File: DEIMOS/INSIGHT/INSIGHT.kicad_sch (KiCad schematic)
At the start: 78 parts, among them J1 Batt, J3 USB_C_Receptacle_USB2.0_16P, J4 Boot, J5 GND, SW3 SW_SPDT, U1 LSM6DS3, U2 MPL3115A2, U3 W25Q128JVSIQ, U4 BNO085, U5 RP2040, U6 Adafruit GPS, U7 MPM3610GQV-Z, U8 RFM95W-915S2, Y1 ABM8-272-T3, Y2 ABS07-32.768KHZ-1-T

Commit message: Finally got to a first footprint with insight it si 3:30 am signing off. There are a few issues and nothing is close to routed yet but it is good enough for now bigest change was putting the rfm95w side by side with the gps foot print is and will proably stay 1.5 x 3. Which is a 0.5 increase on all side to the COMET.
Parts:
- added J2: SMA-J-P-GF-RA-SM1, SMA-J-P-GF-RA-SM1:SAMTEC_SMA-J-P-GF-RA-SM1, symbol SMA-J-P-GF-RA-SM1:SMA-J-P-GF-RA-SM1
- D1, D4: footprint Diode_SMD:D_SOD-323F -> Diode_SMD:D_SOD-110
- J1: footprint Connector_JST:JST_EH_B2B-EH-A_1x02_P2.50mm_Vertical -> TerminalBlock_4Ucon:TerminalBlock_4Ucon_1x02_P3.50mm_Horizontal
- SW3: footprint SPDT:SW_500ASSP1SM6QE -> Button_Switch_SMD:SW_SPDT_CK_JS102011SAQN
- U4: footprint LGA-28_CEV -> footprints:LGA-28_CEV
- U8: footprint (none) -> RF_Module:HOPERF_RFM9XW_SMD
- Y2: footprint ABS07-32.768KHZ-1-T:XTAL_ABS07-32.768KHZ-1-T -> ABS07_32_768KHZ_1_T:XTAL_ABS07-32.768KHZ-1-T
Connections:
- new net: J2.2, J2.3, J2.4, J2.5
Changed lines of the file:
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@@
 	)
 	(rectangle
-		(start 703.58 349.25)
-		(end 824.23 426.72)
+		(start 734.695 349.25)
+		(end 814.705 426.72)
 		(stroke
 			(width 0.508)
@@
 	(text "RFM95W"
 		(exclude_from_sim no)
-		(at 764.032 423.926 0)
+		(at 765.048 414.782 0)
 		(effects
 			(font
@@
 			)
 		)
-		(property "Footprint" "LGA-28_CEV"
+		(property "Footprint" "footprints:LGA-28_CEV"
 			(at 731.52 300.99 0)
 			(hide yes)
@@
 			)
 		)
-		(property "Footprint" "Diode_SMD:D_SOD-323F"
+		(property "Footprint" "Diode_SMD:D_SOD-110"
 			(at 318.77 363.22 0)
 			(hide yes)
@@
 			)
 		)
-		(property "Footprint" "ABS07-32.768KHZ-1-T:XTAL_ABS07-32.768KHZ-1-T"
+		(property "Footprint" "ABS07_32_768KHZ_1_T:XTAL_ABS07-32.768KHZ-1-T"
 			(at 805.18 304.8 0)
 			(hide yes)
@@
 	)
 	(symbol
+		(lib_id "SMA-J-P-GF-RA-SM1:SMA-J-P-GF-RA-SM1")
+		(at 788.67 379.73 0)
+		(mirror y)
+		(unit 1)
+		(body_style 1)
+		(exclude_from_sim no)
+		(in_bom yes)
+		(on_board yes)
+		(in_pos_files yes)
+		(dnp no)
+		(property "Reference" "J2"
+			(at 789.051 370.84 0)
+			(show_name no)
+			(do_not_autoplace no)
+			(effects
+				(font
+					(size 1.27 1.27)
+				)
+			)
+		)
+		(property "Value" "SMA-J-P-GF-RA-SM1"
+			(at 789.051 373.38 0)
+			(show_name no)
+			(do_not_autoplace no)
+			(effects
+				(font
+					(size 1.27 1.27)
+				)
+			)
+		)
+		(property "Footprint" "SMA-J-P-GF-RA-SM1:SAMTEC_SMA-J-P-GF-RA-SM1"
+			(at 788.67 379.73 0)
+			(hide yes)
+			(show_name no)
+			(do_not_autoplace no)
+			(effects
+				(font
+					(size 1.27 1.27)
+				)
+				(justify bottom)
+			)
+		)
+		(property "Datasheet" ""
+			(at 788.67 379.73 0)
+			(hide yes)
+			(show_name no)
+			(do_not_autoplace no)
+			(effects
+				(font
+					(size 1.27 1.27)
+				)
+			)
+		)
+		(property "Description" ""
+			(at 788.67 379.73 0)
+			(hide yes)
+			(show_name no)
+			(do_not_autoplace no)
+			(effects
+				(font
+					(size 1.27 1.27)
+				)
+			)
+		)
+		(property "PARTREV" "D"
+			(at 788.67 379.73 0)
+			(hide yes)
+			(show_name no)
+			(do_not_autoplace no)
+			(effects
+				(font
+					(size 1.27 1.27)
+				)
+				(justify bottom)
+			)
+		)
+		(property "MANUFACTURER" "Samtec"
+			(at 788.67 379.73 0)
+			(hide yes)
+			(show_name no)
+			(do_not_autoplace no)
+			(effects
+				(font
+					(size 1.27 1.27)
+				)
+				(justify bottom)
+			)
+		)
+		(property "MAXIMUM_PACKAGE_HEIGHT" "9.99mm"
+			(at 788.67 379.73 0)
+			(hide yes)
+			(show_name no)
+			(do_not_autoplace no)
+			(effects
+				(font
+					(size 1.27 1.27)
+				)
+				(justify bottom)
+			)
+		)
+		(property "STANDARD" "Manufacturer Recommendations"
+			(at 788.67 379.73 0)
+			(hide yes)
+			(show_name no)
+			(do_not_autoplace no)
+			(effects
+				(font
+					(size 1.27 1.27)
+				)
+				(justify bottom)
+			)
+		)
+		(pin "5"
+		)
+		(pin "4"
+		)
+		(pin "3"
+		)
+		(pin "2"
+		)
+		(pin "1"
+		)
+		(instances
+			(project "INSIGHT"
+				(path "/bf4b749c-e7df-4d18-856a-a4f784e96f1a"
+					(reference "J2")
+					(unit 1)
+				)
+			)
+		)
+	)
+	(symbol
 		(lib_id "Device:C")
 		(at 354.33 386.08 0)
@@
 			)
 		)
-		(property "Footprint" ""
+		(property "Footprint" "RF_Module:HOPERF_RFM9XW_SMD"
 			(at 681.99 342.9 0)
 			(hide yes)
@@
 			)
 		)
-		(property "Footprint" "SPDT:SW_500ASSP1SM6QE"
+		(property "Footprint" "Button_Switch_SMD:SW_SPDT_CK_JS102011SAQN"
 			(at 306.07 339.09 0)
 			(hide yes)
@@
 			)
 		)
-		(property "Footprint" "Connector_JST:JST_EH_B2B-EH-A_1x02_P2.50mm_Vertical"
+		(property "Footprint" "TerminalBlock_4Ucon:TerminalBlock_4Ucon_1x02_P3.50mm_Horizontal"
 			(at 288.29 339.09 0)
 			(hide yes)
@@
 		(exclude_from_sim no)
 		(in_bom yes)
-		(on_board yes)
+		(on_board no)
 		(in_pos_files yes)
 		(dnp no)
@@
 			)
 		)
-		(property "Footprint" "Diode_SMD:D_SOD-323F"
+		(property "Footprint" "Diode_SMD:D_SOD-110"
 			(at 311.15 370.84 0)
 			(hide yes)

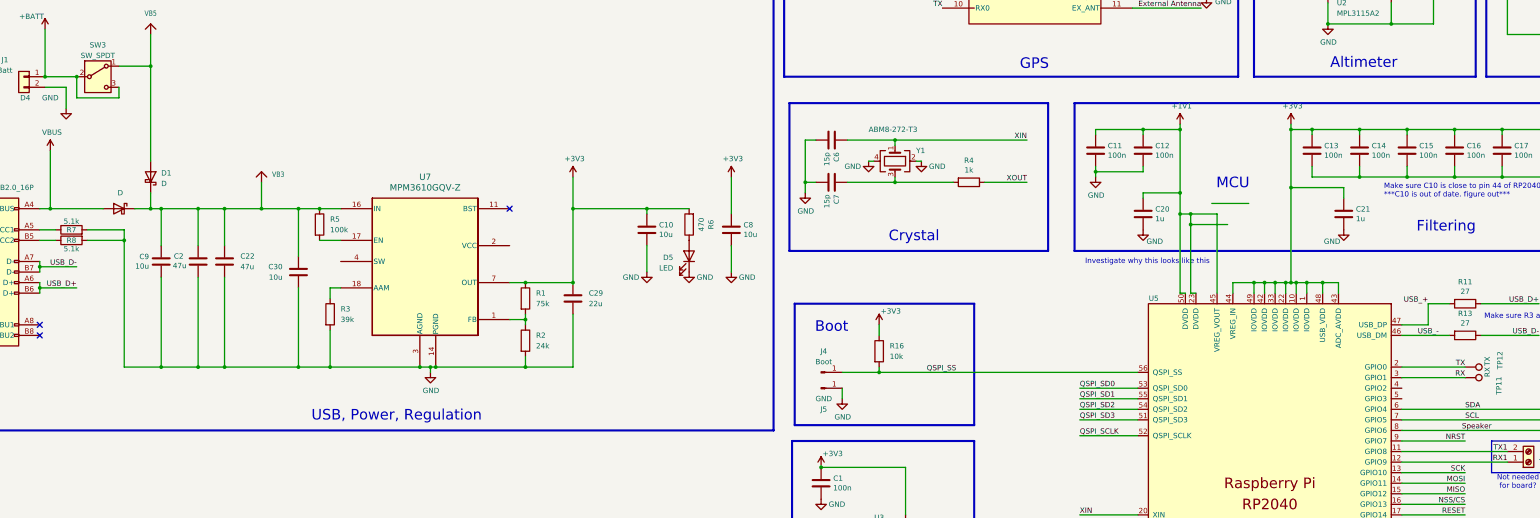
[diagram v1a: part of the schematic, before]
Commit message: Did some prelim routing to see location of items moved speaker and screw terminal
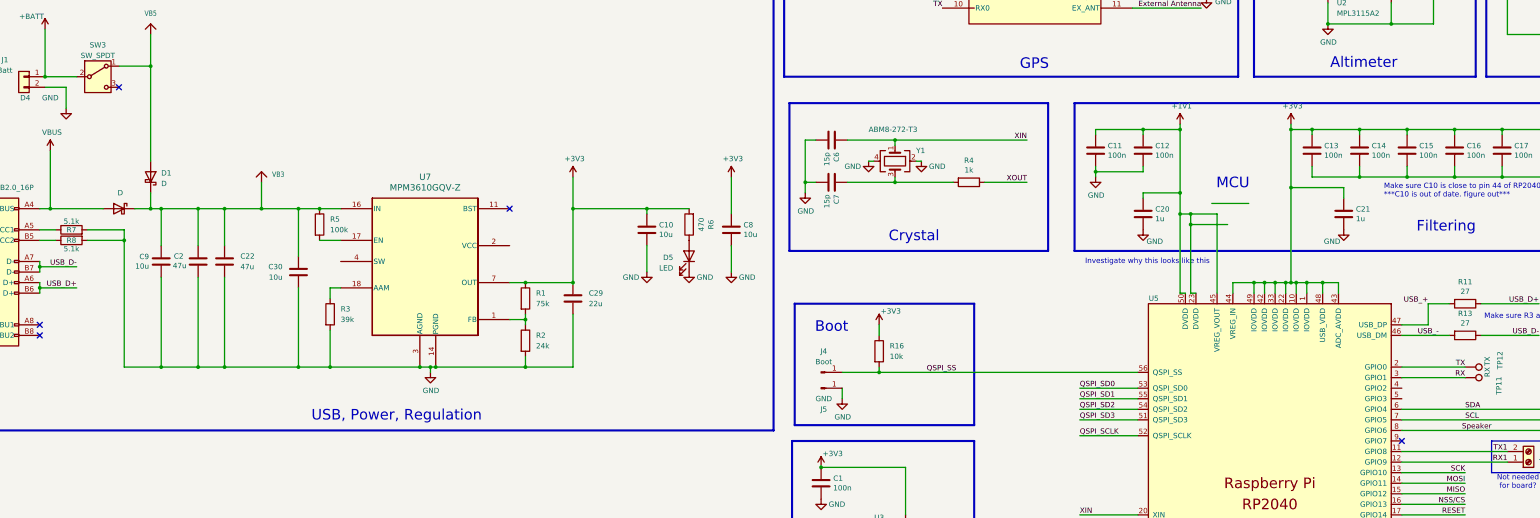
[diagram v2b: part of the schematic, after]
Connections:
- net +BATT: no longer SW3.3 (C)
- net NRST: no longer U5.9 (GPIO7)
- no-connect marks 29 -> 31
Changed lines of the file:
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@@
 	)
 	(junction
-		(at 300.99 339.09)
-		(diameter 0)
-		(color 0 0 0 0)
-	)
-	(junction
 		(at 670.56 297.18)
 		(diameter 0)
@@
 	)
 	(no_connect
+		(at 311.15 341.63)
+	)
+	(no_connect
 		(at 619.76 457.2)
 	)
 	(no_connect
+		(at 619.76 426.72)
+	)
+	(no_connect
 		(at 685.8 307.34)
 	)
@@
 	(wire
 		(pts
-			(xy 311.15 344.17) (xy 300.99 344.17)
-		)
-		(stroke
-			(width 0)
-			(type default)
-		)
-	)
-	(wire
-		(pts
 			(xy 589.28 308.61) (xy 591.82 308.61)
 		)
@@
 	(wire
 		(pts
-			(xy 300.99 339.09) (xy 300.99 344.17)
-		)
-		(stroke
-			(width 0)
-			(type default)
-		)
-	)
-	(wire
-		(pts
 			(xy 480.06 449.58) (xy 490.22 449.58)
 		)
@@
 	(wire
 		(pts
-			(xy 311.15 341.63) (xy 311.15 344.17)
-		)
-		(stroke
-			(width 0)
-			(type default)
-		)
-	)
-	(wire
-		(pts
 			(xy 748.03 377.19) (xy 753.11 377.19)
 		)
@@
 	(wire
 		(pts
-			(xy 619.76 426.72) (xy 635 426.72)
-		)
-		(stroke
-			(width 0)
-			(type default)
-		)
-	)
-	(wire
-		(pts
 			(xy 420.37 408.94) (xy 408.94 408.94)
 		)
@@
 		(effects
 			(font
-				(size 1.27 1.27)
-			)
-			(justify right bottom)
-		)
-	)
-	(label "NRST"
-		(at 635 426.72 180)
-		(effects
-			(font
